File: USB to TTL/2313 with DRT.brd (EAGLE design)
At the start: 15 parts

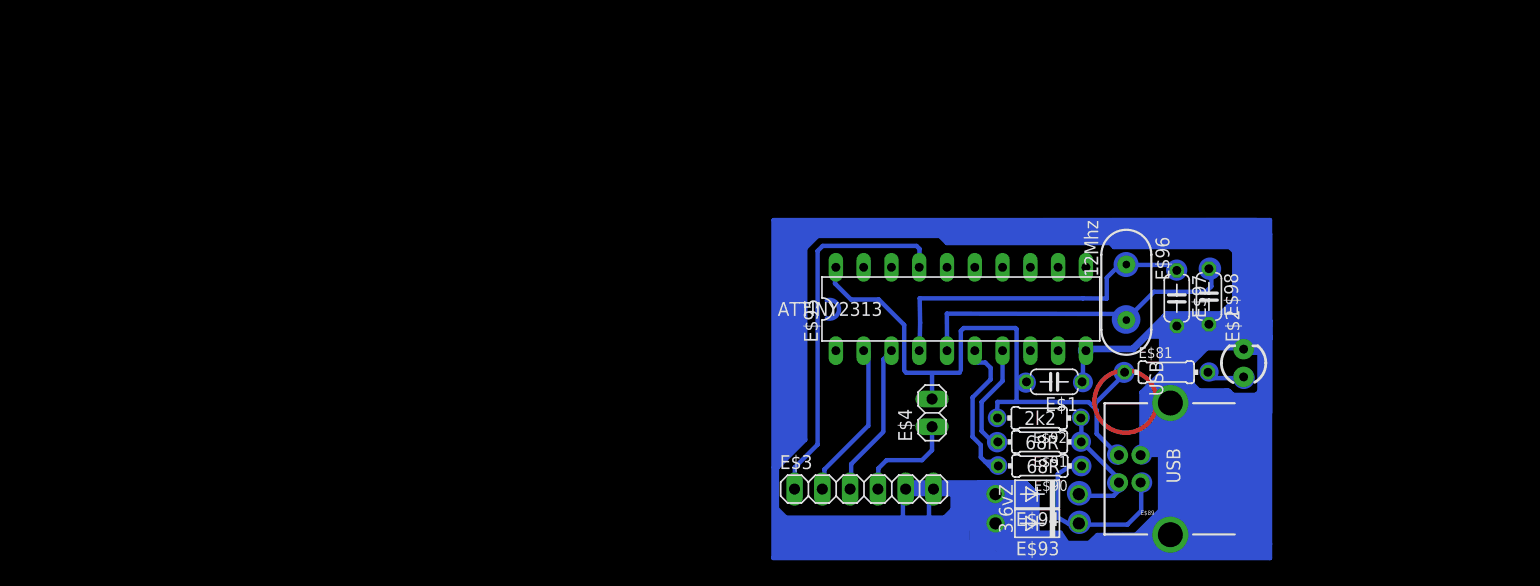
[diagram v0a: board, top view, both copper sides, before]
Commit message: Added Pinout to UD001 (Vishay) after successful test
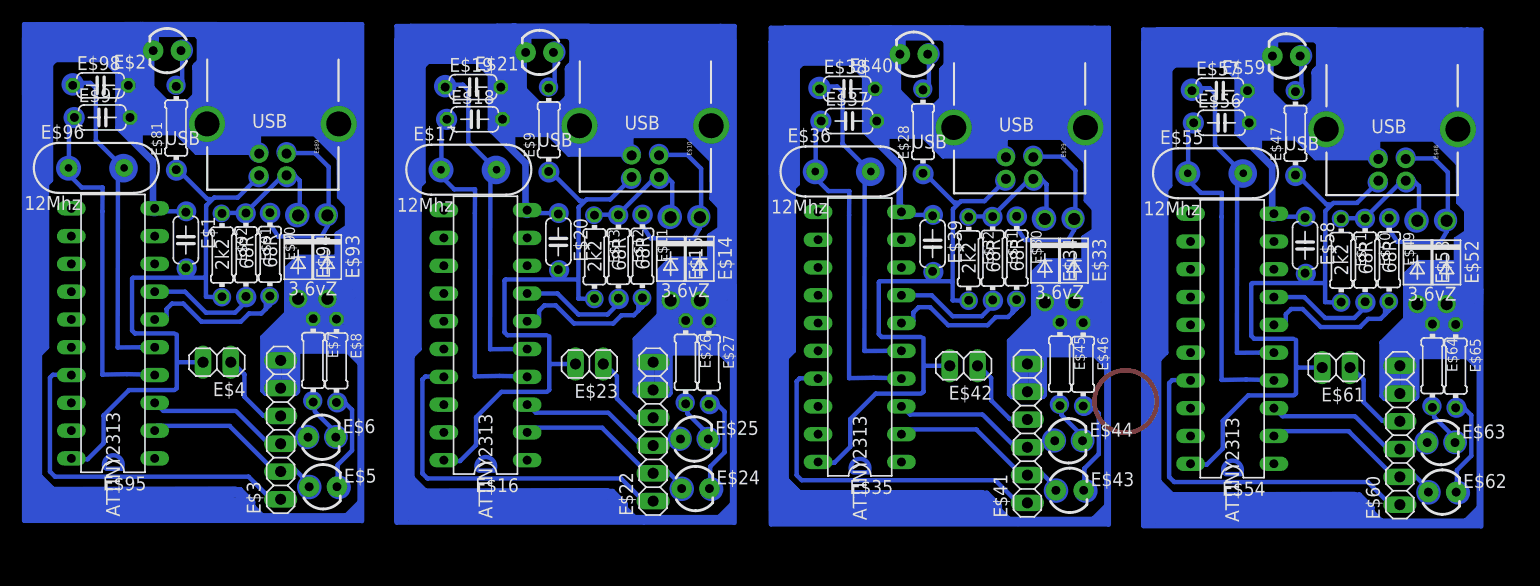
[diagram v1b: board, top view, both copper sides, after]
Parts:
- added E$10, E$29, E$48: (no value), SparkFun-Connectors:USB-B-PTH
- added E$11, E$30, E$49: 68RD+, rcl:0204/7
- added E$12, E$26, E$27, E$31, E$45, E$46, E$50, E$64, E$65, E$7, E$8: 68Rd-, rcl:0204/7
- added E$13, E$28, E$32, E$47, E$51, E$9: 2K2, rcl:0204/7
- added E$14, E$15, E$33, E$34, E$52, E$53: (no value), ref-packages-longpad:DO41-7
- added E$16, E$35, E$54: (no value), 40xx:DIL20
- added E$17, E$36, E$55: (no value), SparkFun-FreqCtrl:HC49US
- added E$18, E$19, E$20, E$37, E$38, E$39, E$56, E$57, E$58: (no value), rcl:C050-024X044
- added E$21, E$24, E$25, E$40, E$43, E$44, E$5, E$59, E$6, E$62, E$63: (no value), SparkFun-LED:LED3MM
- added E$22, E$41, E$60: (no value), pinhead:1X06
- added E$23, E$42, E$61: (no value), pinhead:1X02
- moved E$98 103.2 mm to (9.06, 41.8), turned to 0 degrees
- moved E$2 102.5 mm to (15.1, 45.0), turned to 180 degrees
- moved E$97 99.6 mm to (9.22, 38.9), turned to 0 degrees
- moved E$96 94.9 mm to (8.68, 34.3), turned to 0 degrees
- moved E$81 93.2 mm to (16.0, 37.9), turned to 90 degrees
- moved E$89 84.4 mm to (24.8, 35.6), turned to 270 degrees
- moved E$1 80.4 mm to (16.9, 27.7), turned to 270 degrees
- moved E$95 77.5 mm to (10.2, 19.1), turned to 90 degrees
- moved E$92 76.2 mm to (20.2, 26.3), turned to 270 degrees
- moved E$91 74.5 mm to (22.4, 26.3), turned to 270 degrees
- moved E$90 73.0 mm to (24.6, 26.4), turned to 270 degrees
- moved E$94 71.0 mm to (27.1, 26.1), turned to 270 degrees
- moved E$93 69.3 mm to (29.8, 26.1), turned to 270 degrees
- moved E$4 65.5 mm to (19.7, 16.5), turned to 180 degrees
- moved E$3 53.6 mm to (25.5, 10.3), turned to 90 degrees
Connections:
- new net S$133: E$16.5
- new net S$274: E$35.5
- new net S$402: E$54.5
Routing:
- net S$76: track 175.9 -> 7.77 mm
- net S$462: track 0.00 -> 121.7 mm
- net S$334: track 0.00 -> 121.7 mm
- net S$206: track 0.00 -> 121.7 mm
- net S$428: track 0.00 -> 109.3 mm
- net S$300: track 0.00 -> 109.3 mm
- net S$170: track 0.00 -> 109.3 mm
- net S$336: track 0.00 -> 107.9 mm
- net S$464: track 0.00 -> 107.9 mm
- net S$208: track 0.00 -> 107.9 mm
- net S$243: track 0.00 -> 100.2 mm
- net S$371: track 0.00 -> 100.2 mm
- net S$499: track 0.00 -> 100.2 mm
- net S$74: track 2.53 -> 100.2 mm
- net S$473: track 0.00 -> 85.6 mm
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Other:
- board text removed: "OPENHARDWARE.CO.ZA"
